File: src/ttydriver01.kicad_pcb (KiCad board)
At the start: 2 copper layers, 119.4 x 62.2 mm, 30 parts, among them P1 CONN_01X04, P2 CONN_01X02, P3 CONN_01X02, Q1 IRLB8721PBF, T1 Coilcraft-DA2032, U1 NE555, U2 TPS2030P, U3 CP2102-breakout, U4 G3VM401E, U5 IE0524S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

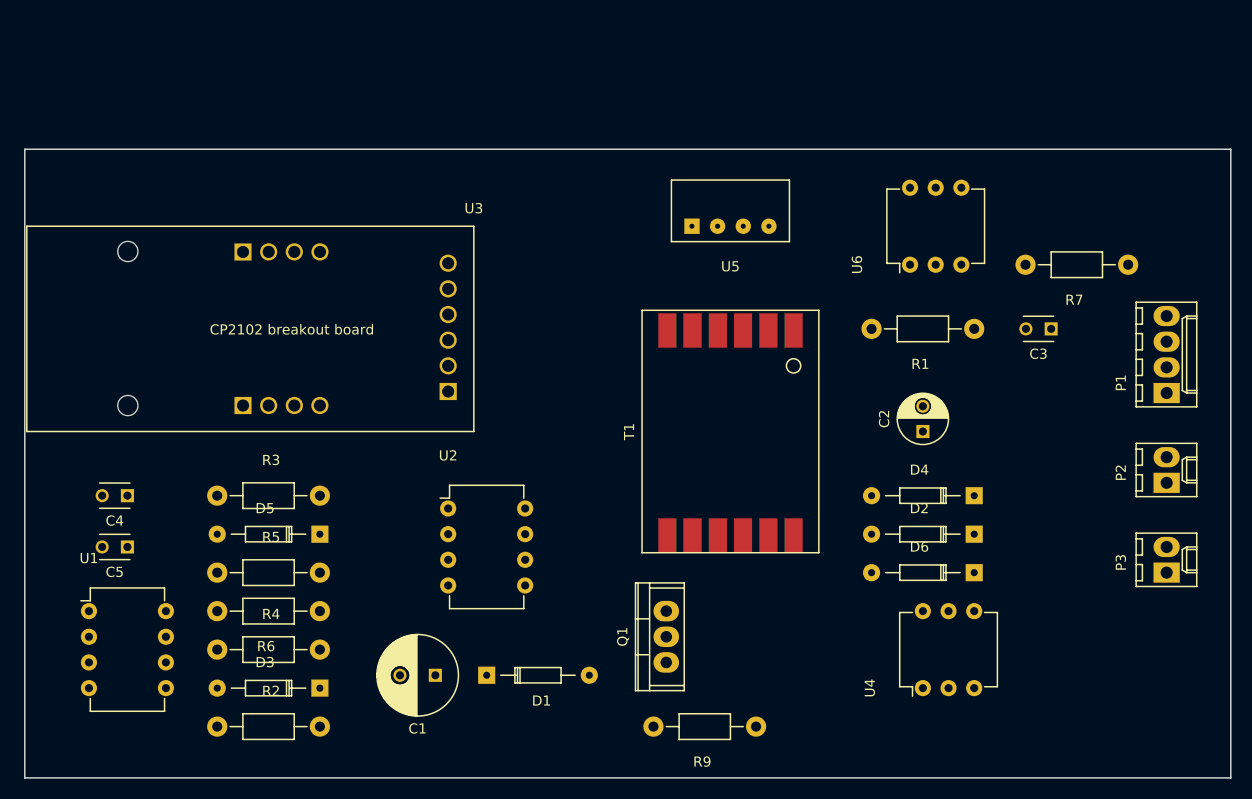
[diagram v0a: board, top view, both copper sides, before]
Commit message: revise front panel connections. Schematic is about done.
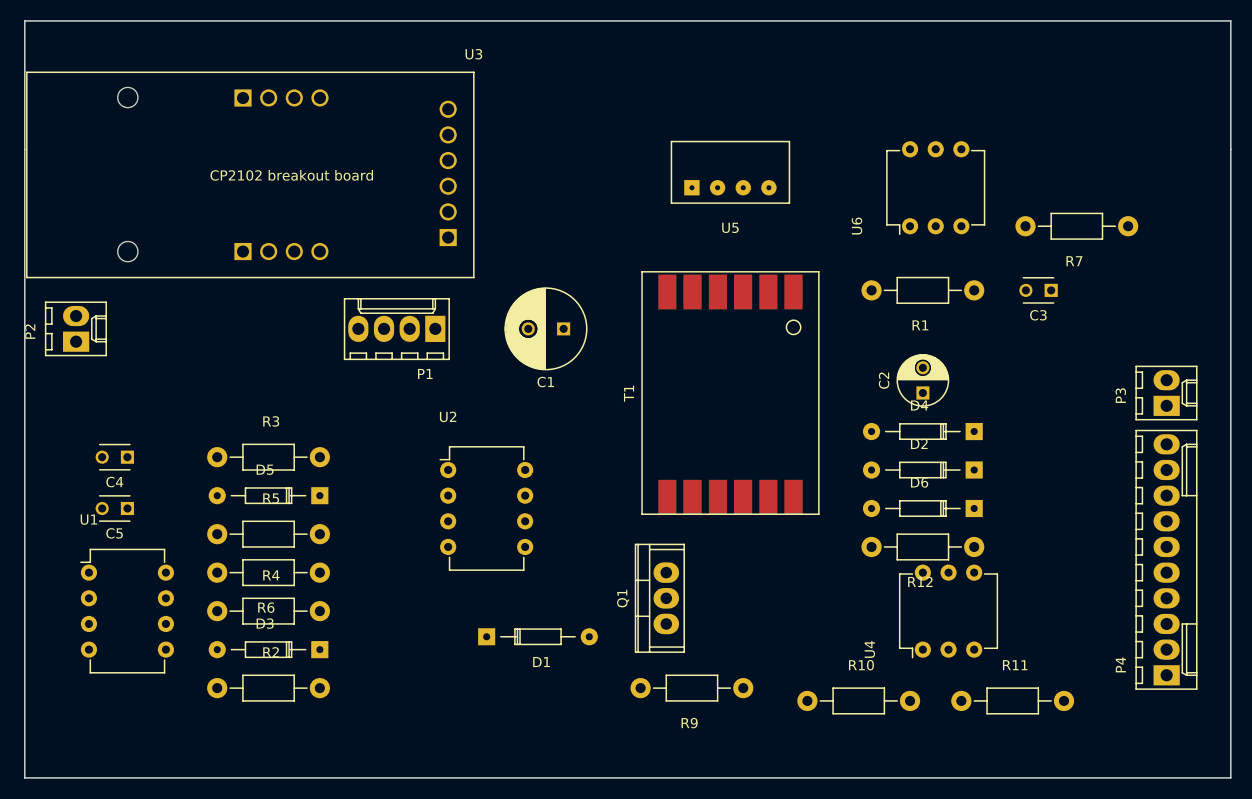
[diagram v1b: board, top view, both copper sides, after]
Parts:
- added P4: CONN_01X10, Connectors_Molex:Molex_KK-6410-10_10x2.54mm_Straight, F.Cu at (168.9, 142.2)
- added R10: 670, Resistors_ThroughHole:Resistor_Horizontal_RM10mm, F.Cu at (133.3, 144.8)
- added R11: 670, Resistors_ThroughHole:Resistor_Horizontal_RM10mm, F.Cu at (148.6, 144.8)
- added R12: 1M, Resistors_ThroughHole:Resistor_Horizontal_RM10mm, F.Cu at (149.9, 129.5)
- moved P2 108.9 mm to (61.0, 109.2)
- moved P1 72.7 mm to (96.5, 108.0), turned to 180 degrees
- moved C1 36.6 mm to (109.2, 108.0)
- moved P3 16.5 mm to (168.9, 115.6)
- moved U3 15.2 mm to (100.3, 82.5)
- moved D2 6.35 mm to (149.9, 121.9)
- moved D6 6.35 mm to (149.9, 125.7)
- moved D4 6.35 mm to (149.9, 118.1)
- moved R9 4.02 mm to (127.0, 143.5)
- moved D5 3.81 mm to (85.1, 124.5)
- moved C2 3.81 mm to (144.8, 114.3)
- moved C3 3.81 mm to (157.5, 104.1)
- moved D1 3.81 mm to (101.6, 138.4)
- moved D3 3.81 mm to (85.1, 139.7)
- moved Q1 3.81 mm to (119.4, 134.6)
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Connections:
- U2 pad 2: Net-(U2-Pad2) -> Net-(P4-Pad2)
- U2 pad 3: Net-(U2-Pad2) -> Net-(P4-Pad2)
- U3 pad 2-4: Net-(U3-Pad2-4) -> VCC
- U3 pad 3-1: Net-(U2-Pad2) -> Net-(P4-Pad1)
- U3 pad 3-4: /RxD -> Net-(P4-Pad6)
- U3 pad 3-5: Net-(P3-Pad2) -> Net-(P4-Pad3)
- U3 pad 3-6: Net-(P3-Pad2) -> Net-(P4-Pad3)
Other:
- board size 119.4 x 62.2 mm -> 119.4 x 74.9 mm

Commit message: Improve board layout. Get HV stuff into clear area.
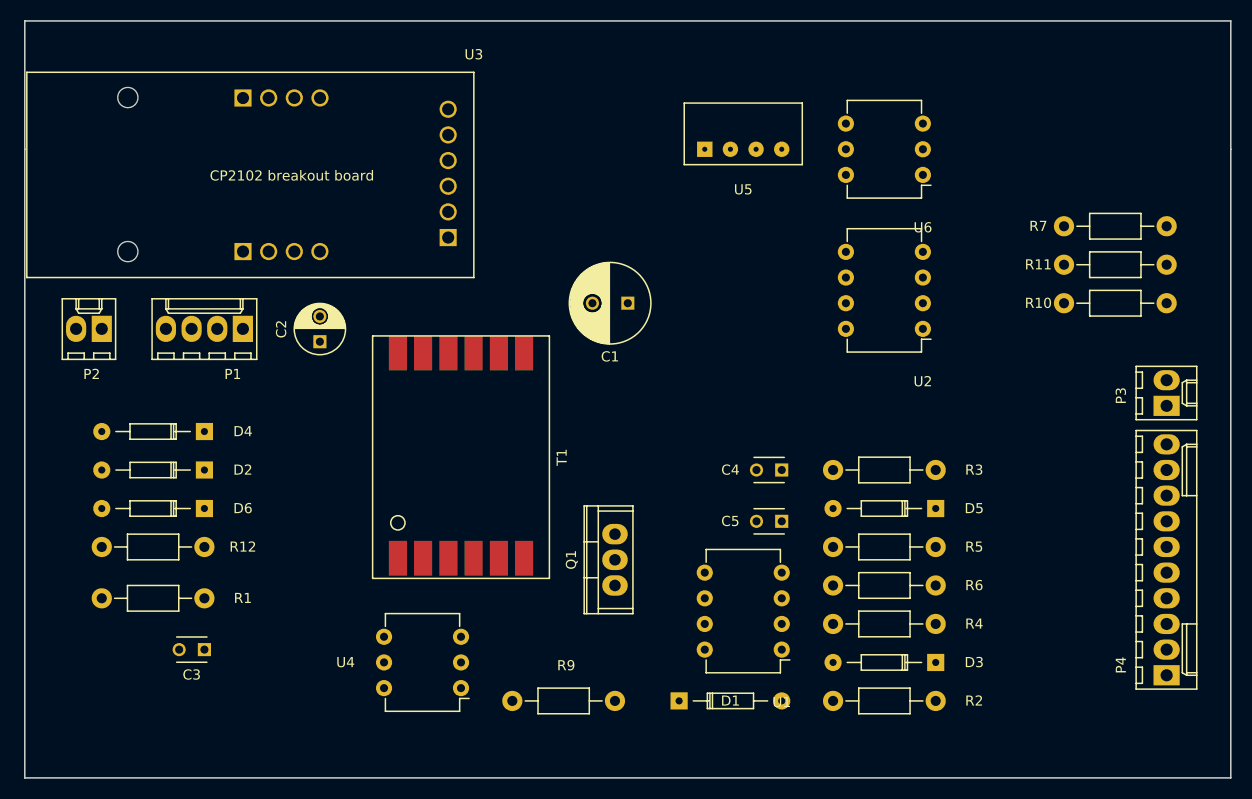
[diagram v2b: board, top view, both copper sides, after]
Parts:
- moved C3 91.1 mm to (73.7, 139.7)
- moved R1 82.1 mm to (73.7, 134.6)
- moved D2 76.2 mm to (73.7, 121.9)
- moved D4 76.2 mm to (73.7, 118.1)
- moved D6 76.2 mm to (73.7, 125.7)
- moved R12 76.2 mm to (73.7, 129.5)
- moved U1 69.0 mm to (130.8, 139.7), turned to 180 degrees
- moved C4 64.8 mm to (130.8, 121.9)
- moved C5 64.8 mm to (130.8, 127.0)
- moved D3 61.0 mm to (146.1, 141.0)
- moved D5 61.0 mm to (146.1, 125.7)
- moved R6 61.0 mm to (146.1, 133.3)
- moved R2 61.0 mm to (135.9, 144.8)
- moved R3 61.0 mm to (135.9, 121.9)
- moved R4 61.0 mm to (135.9, 137.2)
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
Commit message: Everything placed. Ready to start adding tracks
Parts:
- moved P3 8.89 mm to (160.0, 115.6)
- moved P4 8.89 mm to (160.0, 142.2)
- moved C1 7.73 mm to (123.2, 104.1), turned to 0 degrees
- moved D4 5.08 mm to (73.7, 123.2)
- moved R10 3.81 mm to (154.9, 105.4)
- moved R11 3.81 mm to (154.9, 101.6)
- moved R7 3.81 mm to (154.9, 97.8)
- moved D2 2.54 mm to (73.7, 119.4)
- moved R12 1.27 mm to (73.7, 130.8)
- moved C2 1.27 mm to (85.1, 110.5)
- moved D6 1.27 mm to (73.7, 127.0)
- moved P1 1.27 mm to (77.5, 109.2)
- moved P2 1.27 mm to (63.5, 109.2)
- moved U3 1.27 mm to (100.3, 83.8)
- moved C3 1.27 mm to (73.7, 138.4)
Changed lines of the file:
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@@
   )
   (module Capacitors_ThroughHole:C_Radial_D5_L6_P2.5 (layer F.Cu)
-    (at 85.09 109.22 90)
+    (at 85.09 110.49 90)
     (descr "Radial Electrolytic Capacitor Diameter 5mm x Length 6mm, Pitch 2.5mm")
     (tags "Electrolytic Capacitor")
@@
   )
   (module Capacitors_ThroughHole:C_Disc_D3_P2.5 (layer F.Cu)
-    (at 73.66 139.7 180)
+    (at 73.66 138.43 180)
     (descr "Capacitor 3mm Disc, Pitch 2.5mm")
     (tags Capacitor)
@@
   )
   (module Diodes_ThroughHole:Diode_DO-35_SOD27_Horizontal_RM10 (layer F.Cu)
-    (at 73.66 121.92 180)
+    (at 73.66 119.38 180)
     (descr "Diode, DO-35,  SOD27, Horizontal, RM 10mm")
     (tags "Diode, DO-35, SOD27, Horizontal, RM 10mm, 1N4148,")
@@
   )
   (module Diodes_ThroughHole:Diode_DO-35_SOD27_Horizontal_RM10 (layer F.Cu)
-    (at 73.66 118.11 180)
+    (at 73.66 123.19 180)
     (descr "Diode, DO-35,  SOD27, Horizontal, RM 10mm")
     (tags "Diode, DO-35, SOD27, Horizontal, RM 10mm, 1N4148,")
@@
   )
   (module Diodes_ThroughHole:Diode_DO-35_SOD27_Horizontal_RM10 (layer F.Cu)
-    (at 73.66 125.73 180)
+    (at 73.66 127 180)
     (descr "Diode, DO-35,  SOD27, Horizontal, RM 10mm")
     (tags "Diode, DO-35, SOD27, Horizontal, RM 10mm, 1N4148,")
@@
   )
   (module Resistors_ThroughHole:Resistor_Horizontal_RM10mm (layer F.Cu)
-    (at 158.75 97.79)
+    (at 154.94 97.79)
     (descr "Resistor, Axial,  RM 10mm, 1/3W")
     (tags "Resistor Axial RM 10mm 1/3W")
@@
   )
   (module cp2102:CP2102-breakout (layer F.Cu)
-    (at 100.33 82.55 180)
+    (at 100.33 83.82 180)
     (fp_text reference U3 (at 0 1.75 180) (layer F.SilkS)
       (effects (font (size 1 1) (thickness 0.15)))
@@
   )
   (module Connectors_Molex:Molex_KK-6410-04_04x2.54mm_Straight (layer F.Cu)
-    (at 77.47 107.95 180)
+    (at 77.47 109.22 180)
     (descr "Connector Headers with Friction Lock, 22-27-2041, http://www.molex.com/pdm_docs/sd/022272021_sd.pdf")
     (tags "connector molex kk_6410 22-27-2041")
@@
   )
   (module Connectors_Molex:Molex_KK-6410-02_02x2.54mm_Straight (layer F.Cu)
-    (at 63.5 107.95 180)
+    (at 63.5 109.22 180)
     (descr "Connector Headers with Friction Lock, 22-27-2021, http://www.molex.com/pdm_docs/sd/022272021_sd.pdf")
     (tags "connector molex kk_6410 22-27-2021")
@@
   )
   (module Connectors_Molex:Molex_KK-6410-02_02x2.54mm_Straight (layer F.Cu)
-    (at 168.91 115.57 90)
+    (at 160.02 115.57 90)
     (descr "Connector Headers with Friction Lock, 22-27-2021, http://www.molex.com/pdm_docs/sd/022272021_sd.pdf")
     (tags "connector molex kk_6410 22-27-2021")
@@
   )
   (module Capacitors_ThroughHole:C_Radial_D8_L11.5_P3.5 (layer F.Cu)
-    (at 115.57 105.41 180)
+    (at 123.19 104.14)
     (descr "Radial Electrolytic Capacitor Diameter 8mm x Length 11.5mm, Pitch 3.5mm")
     (tags "Electrolytic Capacitor")
-    (fp_text reference C1 (at 1.75 -5.3 180) (layer F.SilkS)
-      (effects (font (size 1 1) (thickness 0.15)))
-    )
-    (fp_text value 220uf (at 1.75 5.3 180) (layer F.Fab)
+    (fp_text reference C1 (at 1.75 -5.3) (layer F.SilkS)
+      (effects (font (size 1 1) (thickness 0.15)))
+    )
+    (fp_text value 220uf (at 1.75 5.3) (layer F.Fab)
       (effects (font (size 1 1) (thickness 0.15)))
     )
@@
     (fp_circle (center 1.75 0) (end 1.75 -4.0375) (layer F.SilkS) (width 0.15))
     (fp_circle (center 1.75 0) (end 1.75 -4.3) (layer F.CrtYd) (width 0.05))
-    (pad 2 thru_hole circle (at 3.5 0 180) (size 1.3 1.3) (drill 0.8) (layers *.Cu *.Mask F.SilkS)
+    (pad 2 thru_hole circle (at 3.5 0) (size 1.3 1.3) (drill 0.8) (layers *.Cu *.Mask F.SilkS)
       (net 2 GND))
-    (pad 1 thru_hole rect (at 0 0 180) (size 1.3 1.3) (drill 0.8) (layers *.Cu *.Mask F.SilkS)
+    (pad 1 thru_hole rect (at 0 0) (size 1.3 1.3) (drill 0.8) (layers *.Cu *.Mask F.SilkS)
       (net 24 "Net-(C1-Pad1)"))
     (model Capacitors_ThroughHole.3dshapes/C_Radial_D8_L11.5_P3.5.wrl
@@
   )
   (module Resistors_ThroughHole:Resistor_Horizontal_RM10mm (layer F.Cu)
-    (at 158.75 105.41)
+    (at 154.94 105.41)
     (descr "Resistor, Axial,  RM 10mm, 1/3W")
     (tags "Resistor Axial RM 10mm 1/3W")
@@
   )
   (module Resistors_ThroughHole:Resistor_Horizontal_RM10mm (layer F.Cu)
-    (at 158.75 101.6)
+    (at 154.94 101.6)
     (descr "Resistor, Axial,  RM 10mm, 1/3W")
     (tags "Resistor Axial RM 10mm 1/3W")
@@
   )
   (module Connectors_Molex:Molex_KK-6410-10_10x2.54mm_Straight (layer F.Cu)
-    (at 168.91 142.24 90)
+    (at 160.02 142.24 90)
     (descr "Connector Headers with Friction Lock, 22-27-2101, http://www.molex.com/pdm_docs/sd/022272021_sd.pdf")
     (tags "connector molex kk_6410 22-27-2101")
@@
   )
   (module Resistors_ThroughHole:Resistor_Horizontal_RM10mm (layer F.Cu)
-    (at 73.66 129.54 180)
+    (at 73.66 130.81 180)
     (descr "Resistor, Axial,  RM 10mm, 1/3W")
     (tags "Resistor Axial RM 10mm 1/3W")
@@
     (polygon
       (pts
-        (xy 55.88 152.4) (xy 175.26 152.4) (xy 175.26 147.32) (xy 55.88 147.32)
+        (xy 95.25 147.32) (xy 175.26 147.32) (xy 175.26 152.4) (xy 55.88 152.4) (xy 55.88 104.14)
+        (xy 95.25 104.14) (xy 95.25 147.32)
       )
     )

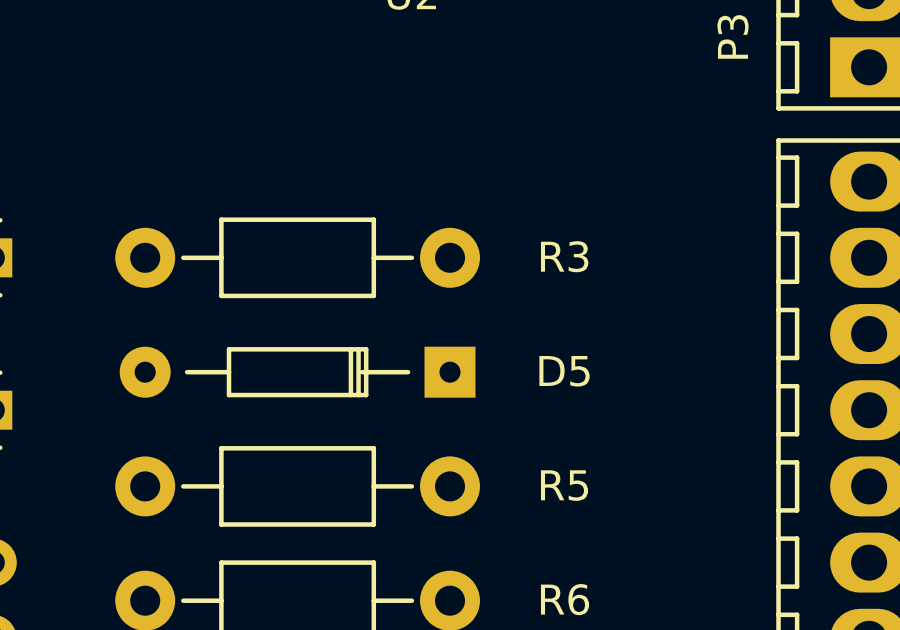
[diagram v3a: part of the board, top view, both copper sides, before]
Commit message: Connectivity on board doesn't match connectivity on schematic
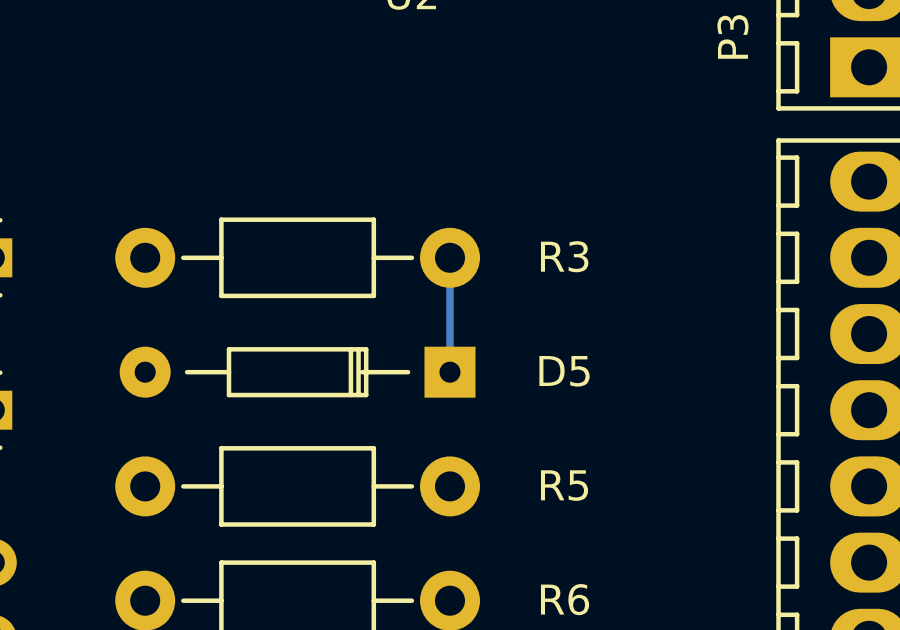
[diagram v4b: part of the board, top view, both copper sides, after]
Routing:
- net Net-(D5-Pad1): track 0.00 -> 3.81 mm
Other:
- net class PWR added: clearance 0.5, trace_width 1, via_dia 0.6, via_drill 0.4
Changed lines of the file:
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@@
   (general
     (links 78)
-    (no_connects 78)
+    (no_connects 77)
     (area 55.804999 77.394999 175.335001 152.475001)
     (thickness 1.6)
     (drawings 8)
-    (tracks 0)
+    (tracks 2)
     (zones 0)
     (modules 34)
@@
     (add_net /RxD)
     (add_net /TxD)
-    (add_net GND)
-    (add_net "Net-(C1-Pad1)")
-    (add_net "Net-(C2-Pad1)")
-    (add_net "Net-(C2-Pad2)")
     (add_net "Net-(C3-Pad1)")
     (add_net "Net-(C3-Pad2)")
@@
     (add_net "Net-(P4-Pad8)")
     (add_net "Net-(P4-Pad9)")
-    (add_net "Net-(Q1-Pad2)")
-    (add_net "Net-(Q1-Pad3)")
     (add_net "Net-(R4-Pad1)")
     (add_net "Net-(R7-Pad2)")
@@
     (add_net "Net-(U5-Pad3)")
     (add_net "Net-(U6-Pad3)")
+  )
+  (net_class PWR ""
+    (clearance 0.5)
+    (trace_width 1)
+    (via_dia 0.6)
+    (via_drill 0.4)
+    (uvia_dia 0.3)
+    (uvia_drill 0.1)
+    (add_net GND)
+    (add_net "Net-(C1-Pad1)")
+    (add_net "Net-(C2-Pad1)")
+    (add_net "Net-(C2-Pad2)")
+    (add_net "Net-(Q1-Pad2)")
+    (add_net "Net-(Q1-Pad3)")
     (add_net VCC)
   )
@@
   (gr_line (start 55.88 152.4) (end 175.26 152.4) (angle 90) (layer Edge.Cuts) (width 0.15))
   (gr_line (start 175.26 90.17) (end 175.26 152.4) (angle 90) (layer Edge.Cuts) (width 0.15))
+  (segment (start 146.05 121.92) (end 146.05 125.73202) (width 0.25) (layer B.Cu) (net 7))
+  (segment (start 146.05 125.73202) (end 146.04948 125.73254) (width 0.25) (layer B.Cu) (net 7))
   (zone (net 0) (net_name "") (layer F.Cu) (hatch edge 0.508)
     (connect_pads (clearance 0.508))

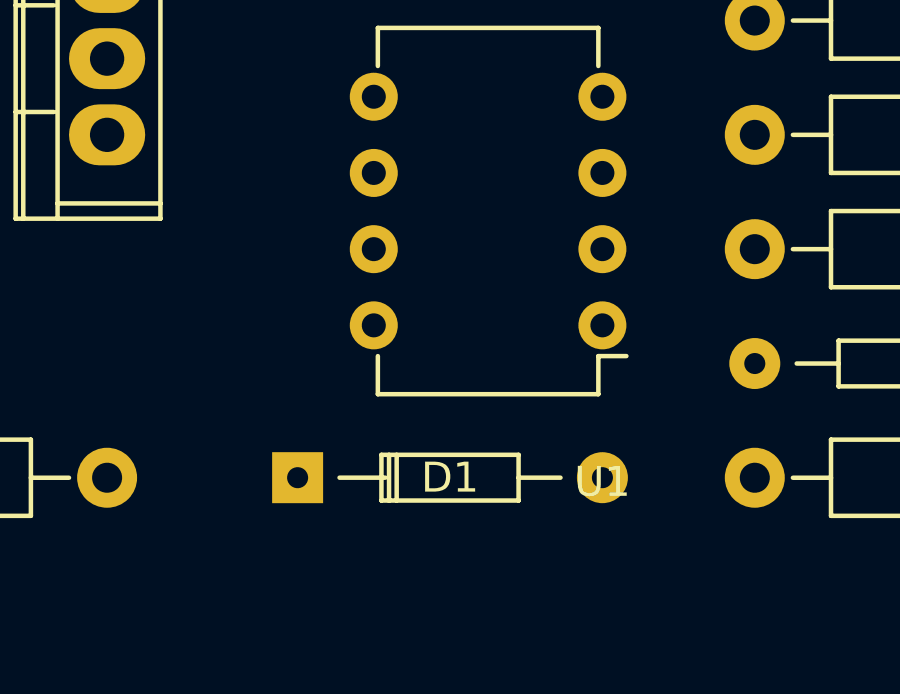
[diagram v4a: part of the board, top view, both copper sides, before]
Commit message: Relabled some nets - fixed connectivity
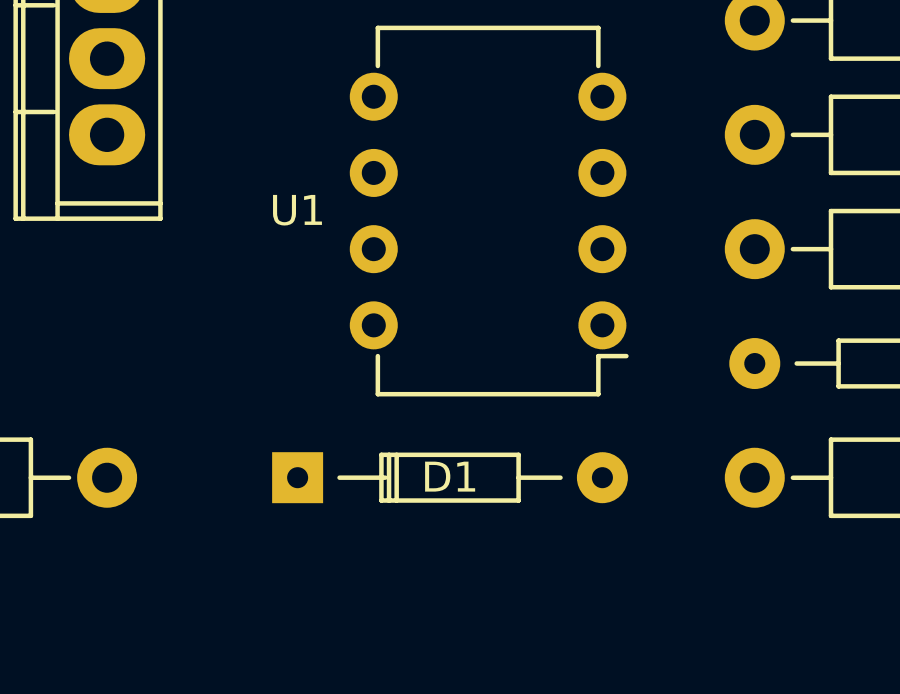
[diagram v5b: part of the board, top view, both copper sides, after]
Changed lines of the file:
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@@
       (effects (font (size 1 1) (thickness 0.15)))
     )
-    (fp_text value D (at 4.41452 -3.55854) (layer F.Fab)
+    (fp_text value D (at 7.62 1.27) (layer F.Fab)
       (effects (font (size 1 1) (thickness 0.15)))
     )
@@
     (descr "8-lead dip package, row spacing 7.62 mm (300 mils)")
     (tags "dil dip 2.54 300")
-    (fp_text reference U1 (at 0 -5.22 180) (layer F.SilkS)
-      (effects (font (size 1 1) (thickness 0.15)))
-    )
-    (fp_text value NE555 (at 0 -3.72 180) (layer F.Fab)
-      (effects (font (size 1 1) (thickness 0.15)))
-    )
+    (fp_text reference U1 (at 10.16 3.81 180) (layer F.SilkS)
+      (effects (font (size 1 1) (thickness 0.15)))
+    )
+    (fp_text value NE555 (at 3.81 1.27 180) (layer F.Fab)
+      (effects (font (size 1 1) (thickness 0.15)))
+    )
